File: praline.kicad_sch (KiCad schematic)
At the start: 0 parts

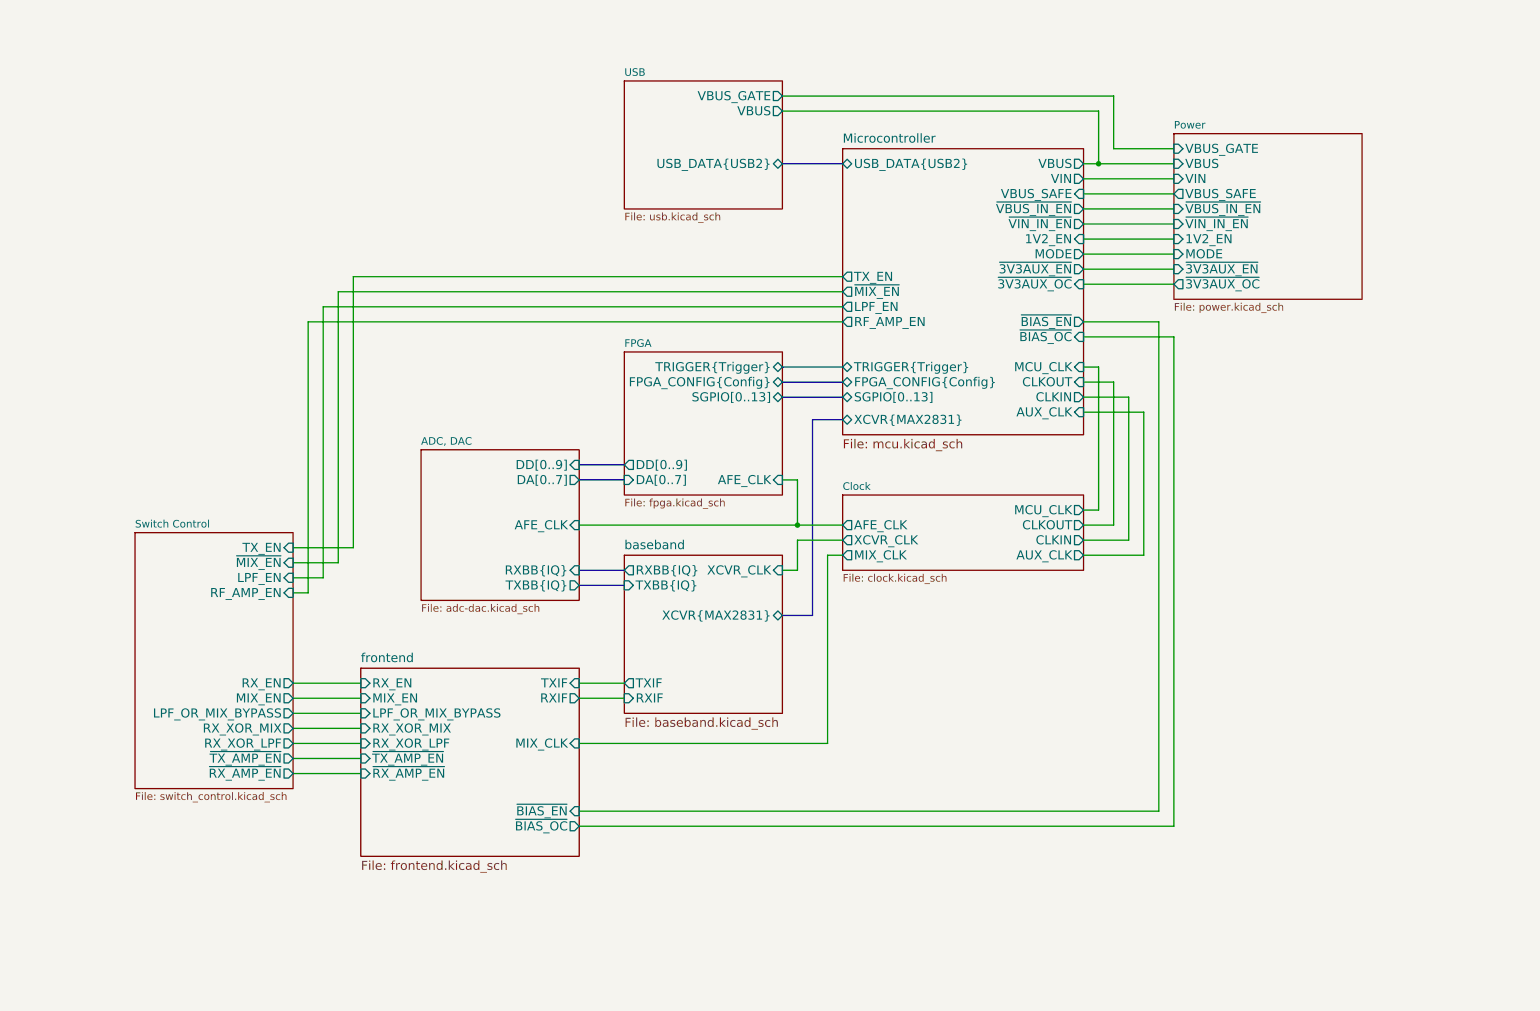
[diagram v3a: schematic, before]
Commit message: Multiplex clock I/O signals
- Allow switching of CLKIN and CLKOUT ports to trigger I/O and other signals
- Add SCT_CLK
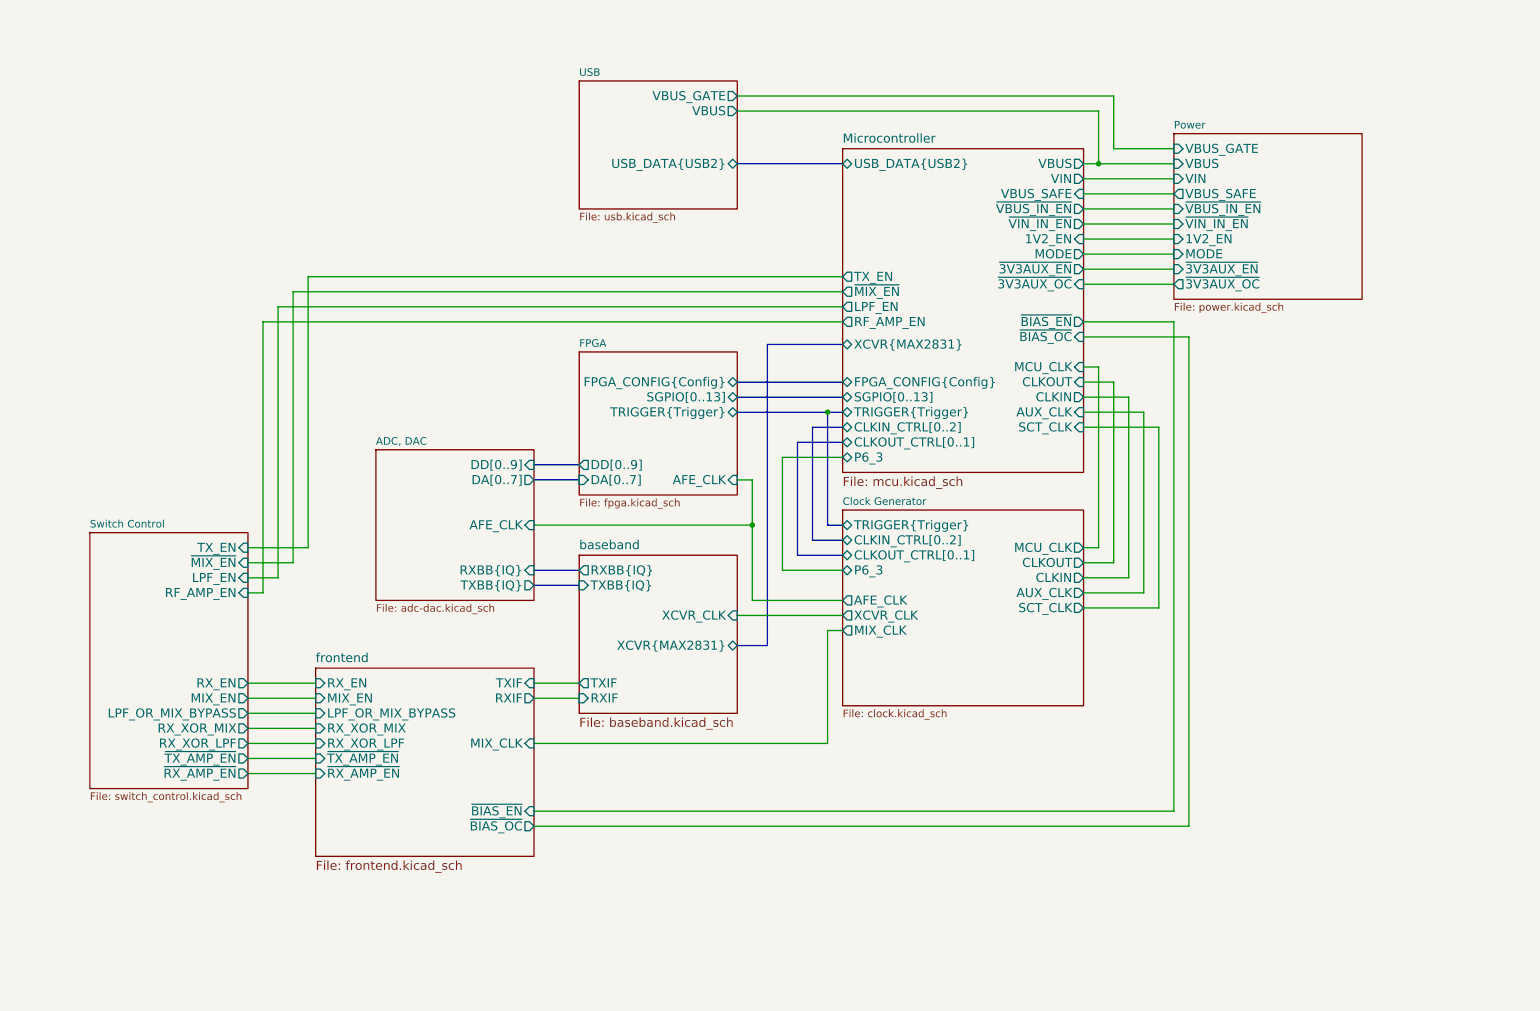
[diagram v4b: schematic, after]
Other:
- sheet Clock renamed Clock Generator
- sheet Clock Generator ports: added CLKIN_CTRL[0..2], CLKOUT_CTRL[0..1], P6_3, SCT_CLK, TRIGGER{Trigger}; removed none
- sheet Microcontroller ports: added CLKIN_CTRL[0..2], CLKOUT_CTRL[0..1], P6_3, SCT_CLK; removed none

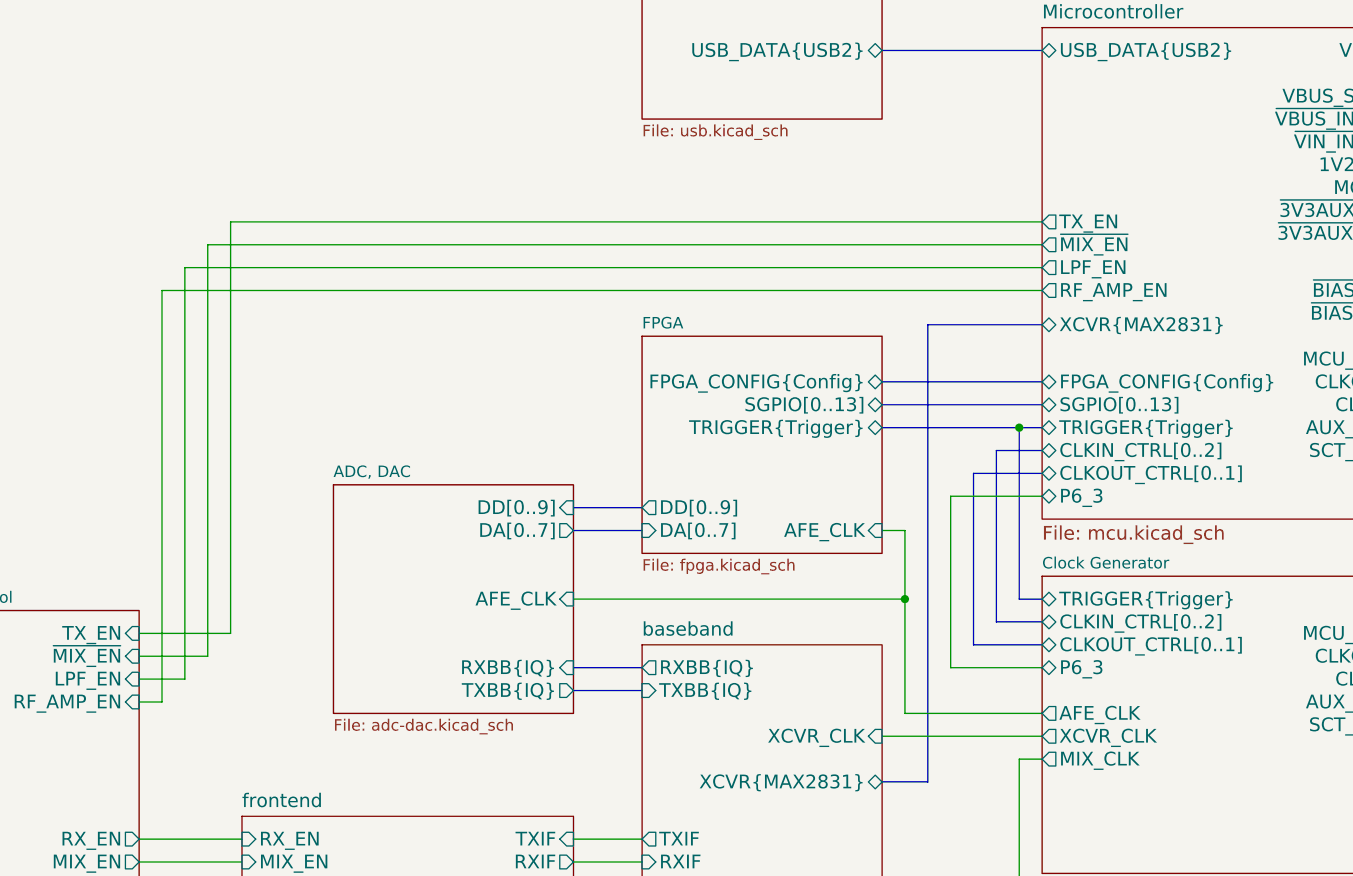
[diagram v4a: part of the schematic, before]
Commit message: Add narrowband anti-aliasing filter
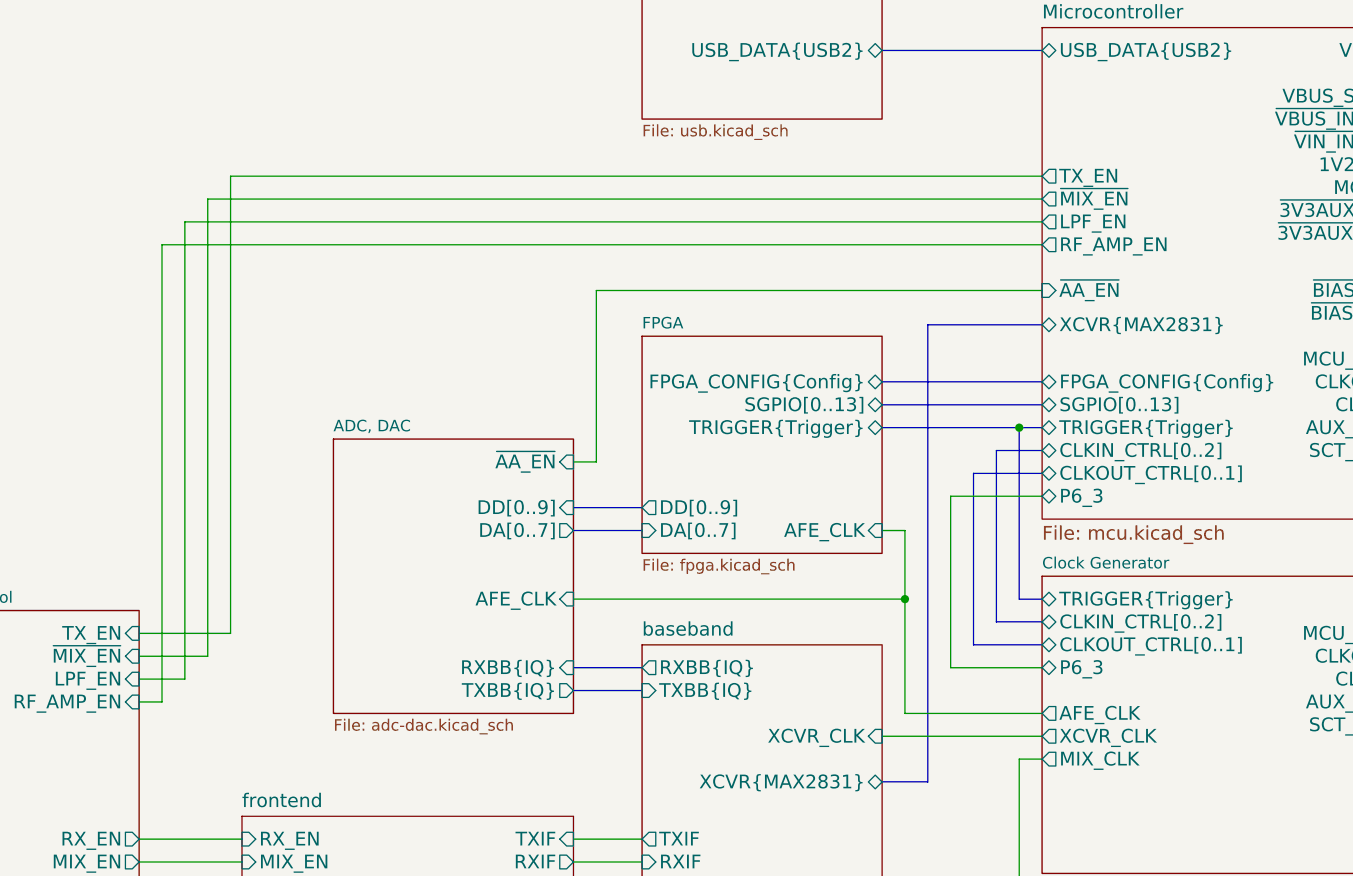
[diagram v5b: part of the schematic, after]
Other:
- sheet ADC, DAC ports: added ~{AA_EN}; removed none
- sheet Microcontroller ports: added ~{AA_EN}; removed none
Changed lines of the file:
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@@
 	(wire
 		(pts
-			(xy 74.93 58.42) (xy 165.1 58.42)
+			(xy 74.93 53.34) (xy 165.1 53.34)
 		)
 		(stroke
@@
 	(wire
 		(pts
+			(xy 115.57 85.09) (xy 113.03 85.09)
+		)
+		(stroke
+			(width 0)
+			(type default)
+		)
+	)
+	(wire
+		(pts
 			(xy 205.74 39.37) (xy 208.28 39.37)
 		)
@@
 	(wire
 		(pts
-			(xy 72.39 60.96) (xy 72.39 106.68)
+			(xy 165.1 66.04) (xy 115.57 66.04)
+		)
+		(stroke
+			(width 0)
+			(type default)
+		)
+	)
+	(wire
+		(pts
+			(xy 72.39 55.88) (xy 72.39 106.68)
 		)
 		(stroke
@@
 	(wire
 		(pts
+			(xy 115.57 66.04) (xy 115.57 85.09)
+		)
+		(stroke
+			(width 0)
+			(type default)
+		)
+	)
+	(wire
+		(pts
 			(xy 205.74 78.74) (xy 213.36 78.74)
 		)
@@
 	(wire
 		(pts
-			(xy 165.1 60.96) (xy 72.39 60.96)
+			(xy 165.1 55.88) (xy 72.39 55.88)
 		)
 		(stroke
@@
 	(wire
 		(pts
-			(xy 165.1 66.04) (xy 67.31 66.04)
+			(xy 165.1 60.96) (xy 67.31 60.96)
 		)
 		(stroke
@@
 	(wire
 		(pts
-			(xy 69.85 63.5) (xy 165.1 63.5)
+			(xy 69.85 58.42) (xy 165.1 58.42)
 		)
 		(stroke
@@
 	(wire
 		(pts
-			(xy 74.93 104.14) (xy 74.93 58.42)
-		)
-		(stroke
-			(width 0)
-			(type default)
-		)
-	)
-	(wire
-		(pts
-			(xy 67.31 66.04) (xy 67.31 111.76)
+			(xy 74.93 104.14) (xy 74.93 53.34)
+		)
+		(stroke
+			(width 0)
+			(type default)
+		)
+	)
+	(wire
+		(pts
+			(xy 67.31 60.96) (xy 67.31 111.76)
 		)
 		(stroke
@@
 	(wire
 		(pts
-			(xy 69.85 109.22) (xy 69.85 63.5)
+			(xy 69.85 109.22) (xy 69.85 58.42)
 		)
 		(stroke
@@
 		)
 		(pin "LPF_EN" output
-			(at 165.1 63.5 180)
+			(at 165.1 58.42 180)
 			(effects
 				(font
@@
 		)
 		(pin "RF_AMP_EN" output
-			(at 165.1 66.04 180)
+			(at 165.1 60.96 180)
 			(effects
 				(font
@@
 		)
 		(pin "TX_EN" output
-			(at 165.1 58.42 180)
+			(at 165.1 53.34 180)
 			(effects
 				(font
@@
 		)
 		(pin "~{MIX_EN}" output
-			(at 165.1 60.96 180)
+			(at 165.1 55.88 180)
 			(effects
 				(font
@@
 				)
 				(justify right)
+			)
+		)
+		(pin "~{AA_EN}" input
+			(at 165.1 66.04 180)
+			(effects
+				(font
+					(size 1.524 1.524)
+				)
+				(justify left)
 			)
 		)
@@
 	)
 	(sheet
-		(at 86.36 87.63)
-		(size 26.67 25.4)
+		(at 86.36 82.55)
+		(size 26.67 30.48)
 		(fields_autoplaced yes)
 		(stroke
@@
 		)
 		(property "Sheetname" "ADC, DAC"
-			(at 86.36 86.9184 0)
+			(at 86.36 81.8384 0)
 			(effects
 				(font
@@
 			(effects
 				(font
+					(size 1.524 1.524)
+				)
+				(justify right)
+			)
+		)
+		(pin "~{AA_EN}" input
+			(at 113.03 85.09 0)
+			(effects
+				(font

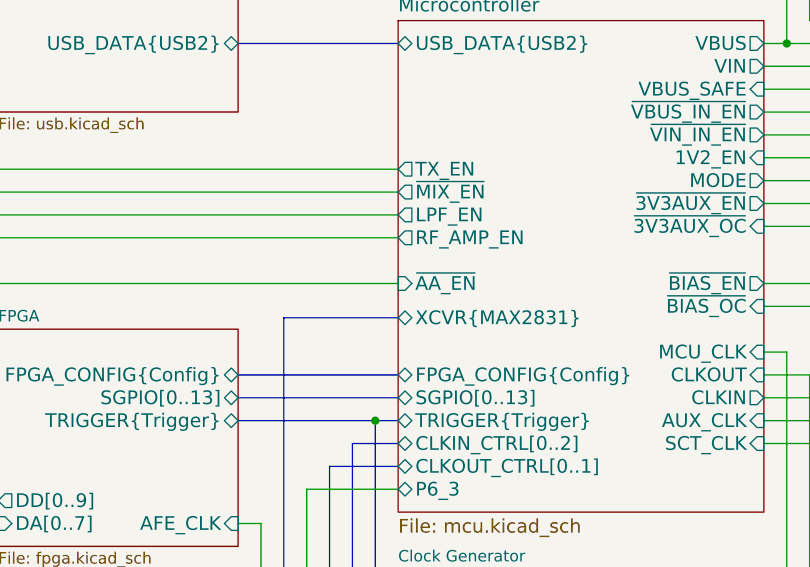
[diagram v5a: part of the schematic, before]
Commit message: Improve baseband TX attenuation options
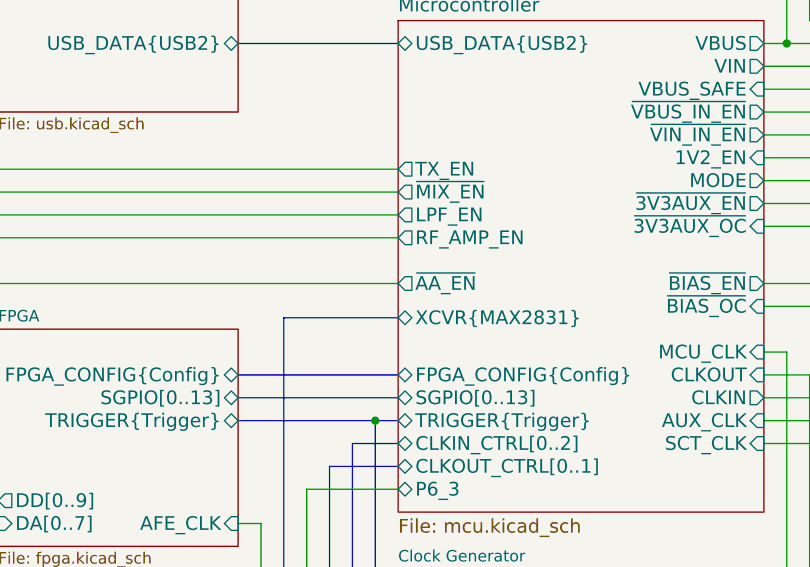
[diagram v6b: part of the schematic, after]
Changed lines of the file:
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@@
 			)
 		)
-		(pin "~{AA_EN}" input
+		(pin "~{AA_EN}" output
 			(at 165.1 66.04 180)
 			(effects
